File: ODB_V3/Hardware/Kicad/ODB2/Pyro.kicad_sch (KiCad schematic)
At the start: 51 parts, among them J9 Screw_Terminal_01x08, Q2 SI7617DN-T1-GE3, Q3 MMBT3904, U10 SI5442DU-T1-GE3, U11 SI5442DU-T1-GE3, U12 SI5442DU-T1-GE3, U6 LM339, U7 SI5442DU-T1-GE3

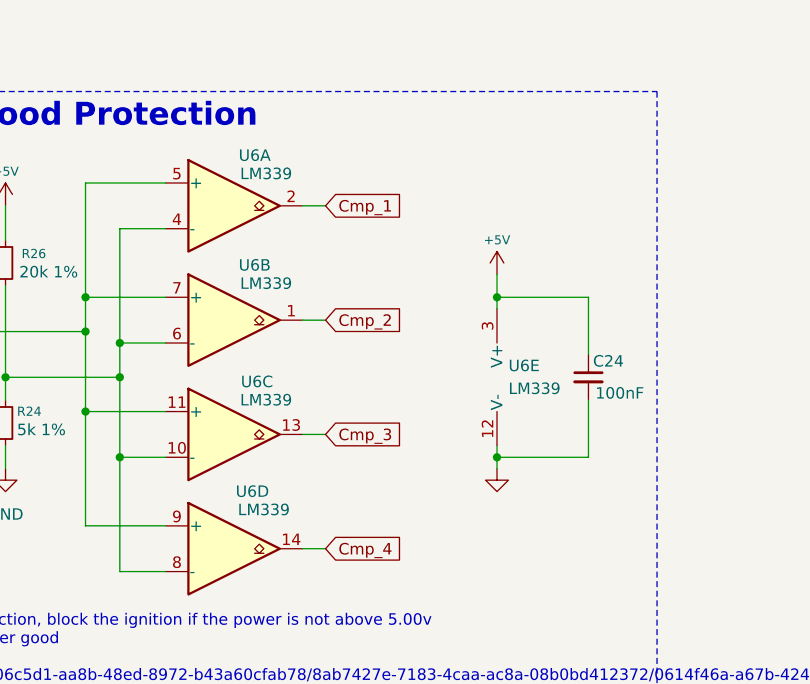
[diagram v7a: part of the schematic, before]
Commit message: wip :fix solder paste reduction for large footprints
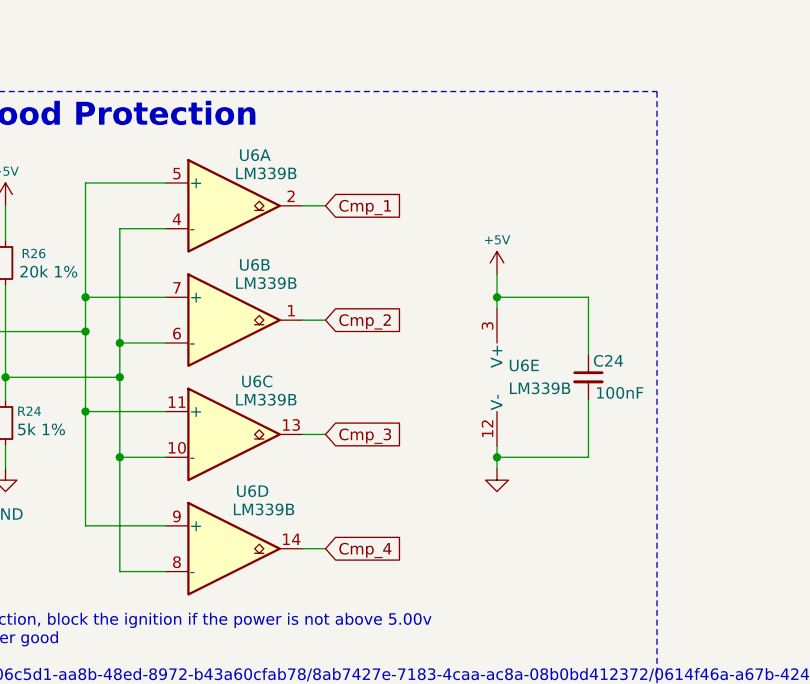
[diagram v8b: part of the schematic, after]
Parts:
- U6: value LM339 -> LM339B; DigiKey_Part_Number 296-1013-1-ND -> 296-LM339BIPWRCT-ND; Manufacturer_Part_Number (none) -> LM339BIPWR; Purchase-URL https://www.digikey.ca/en/products/detail/texas-instruments/LM339DR/276657 -> https://www.digikey.ca/en/products/detail/texas-instruments/LM339BIPWR/21298817
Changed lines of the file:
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@@
 			)
 		)
-		(property "Value" "LM339"
+		(property "Value" "LM339B"
 			(at 61.976 42.926 0)
 			(effects
@@
 			)
 		)
-		(property "DigiKey_Part_Number" "296-1013-1-ND"
+		(property "DigiKey_Part_Number" "296-LM339BIPWRCT-ND"
 			(at 58.42 46.99 0)
 			(effects
@@
 			)
 		)
-		(property "Purchase-URL" "https://www.digikey.ca/en/products/detail/texas-instruments/LM339DR/276657"
+		(property "Purchase-URL" "https://www.digikey.ca/en/products/detail/texas-instruments/LM339BIPWR/21298817"
 			(at 58.42 46.99 0)
 			(effects
@@
 			)
 		)
+		(property "Manufacturer_Part_Number" "LM339BIPWR"
+			(at 58.42 46.99 0)
+			(effects
+				(font
+					(size 1.27 1.27)
+				)
+				(hide yes)
+			)
+		)
 		(pin "5"
 		)
@@
 			)
 		)
-		(property "Value" "LM339"
+		(property "Value" "LM339B"
 			(at 61.722 68.072 0)
 			(effects
@@
 			)
 		)
-		(property "DigiKey_Part_Number" "296-1013-1-ND"
+		(property "DigiKey_Part_Number" "296-LM339BIPWRCT-ND"
 			(at 58.42 72.39 0)
 			(effects
@@
 			)
 		)
-		(property "Purchase-URL" "https://www.digikey.ca/en/products/detail/texas-instruments/LM339DR/276657"
+		(property "Purchase-URL" "https://www.digikey.ca/en/products/detail/texas-instruments/LM339BIPWR/21298817"
 			(at 58.42 72.39 0)
 			(effects
@@
 			)
 		)
+		(property "Manufacturer_Part_Number" "LM339BIPWR"
+			(at 58.42 72.39 0)
+			(effects
+				(font
+					(size 1.27 1.27)
+				)
+				(hide yes)
+			)
+		)
 		(pin "5"
 		)
@@
 			)
 		)
-		(property "Value" "LM339"
+		(property "Value" "LM339B"
 			(at 61.976 30.734 0)
 			(effects
@@
 			)
 		)
-		(property "DigiKey_Part_Number" "296-1013-1-ND"
+		(property "DigiKey_Part_Number" "296-LM339BIPWRCT-ND"
 			(at 58.42 34.29 0)
 			(effects
@@
 			)
 		)
-		(property "Purchase-URL" "https://www.digikey.ca/en/products/detail/texas-instruments/LM339DR/276657"
+		(property "Purchase-URL" "https://www.digikey.ca/en/products/detail/texas-instruments/LM339BIPWR/21298817"
 			(at 58.42 34.29 0)
 			(effects
@@
 			)
 		)
+		(property "Manufacturer_Part_Number" "LM339BIPWR"
+			(at 58.42 34.29 0)
+			(effects
+				(font
+					(size 1.27 1.27)
+				)
+				(hide yes)
+			)
+		)
 		(pin "5"
 		)
@@
 			)
 		)
-		(property "Value" "LM339"
+		(property "Value" "LM339B"
 			(at 88.9 54.6099 0)
 			(effects
@@
 			)
 		)
-		(property "DigiKey_Part_Number" "296-1013-1-ND"
+		(property "DigiKey_Part_Number" "296-LM339BIPWRCT-ND"
 			(at 90.17 53.34 0)
 			(effects
@@
 			)
 		)
-		(property "Purchase-URL" "https://www.digikey.ca/en/products/detail/texas-instruments/LM339DR/276657"
+		(property "Purchase-URL" "https://www.digikey.ca/en/products/detail/texas-instruments/LM339BIPWR/21298817"
 			(at 90.17 53.34 0)
 			(effects
@@
 			)
 		)
+		(property "Manufacturer_Part_Number" "LM339BIPWR"
+			(at 90.17 53.34 0)
+			(effects
+				(font
+					(size 1.27 1.27)
+				)
+				(hide yes)
+			)
+		)
 		(pin "7"
 		)
@@
 			)
 		)
-		(property "Value" "LM339"
+		(property "Value" "LM339B"
 			(at 61.976 55.88 0)
 			(effects
@@
 			)
 		)
-		(property "DigiKey_Part_Number" "296-1013-1-ND"
+		(property "DigiKey_Part_Number" "296-LM339BIPWRCT-ND"
 			(at 58.42 59.69 0)
 			(effects
@@
 			)
 		)
-		(property "Purchase-URL" "https://www.digikey.ca/en/products/detail/texas-instruments/LM339DR/276657"
+		(property "Purchase-URL" "https://www.digikey.ca/en/products/detail/texas-instruments/LM339BIPWR/21298817"
 			(at 58.42 59.69 0)
 			(effects
@@
 			(at 58.42 59.69 0)
 			(effects
+				(font
+					(size 1.27 1.27)
+				)
+				(hide yes)
+			)
+		)
+		(property "Manufacturer_Part_Number" "LM339BIPWR"
+			(at 58.42 59.69 0)
+			(effects
